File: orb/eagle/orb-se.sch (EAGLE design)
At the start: 27 parts, among them J1 MICRO USB, Q1 12MHZ, T1 DMG2302U, T2 DMG2302U, T3 DMG2302U, U1 ATINY44A

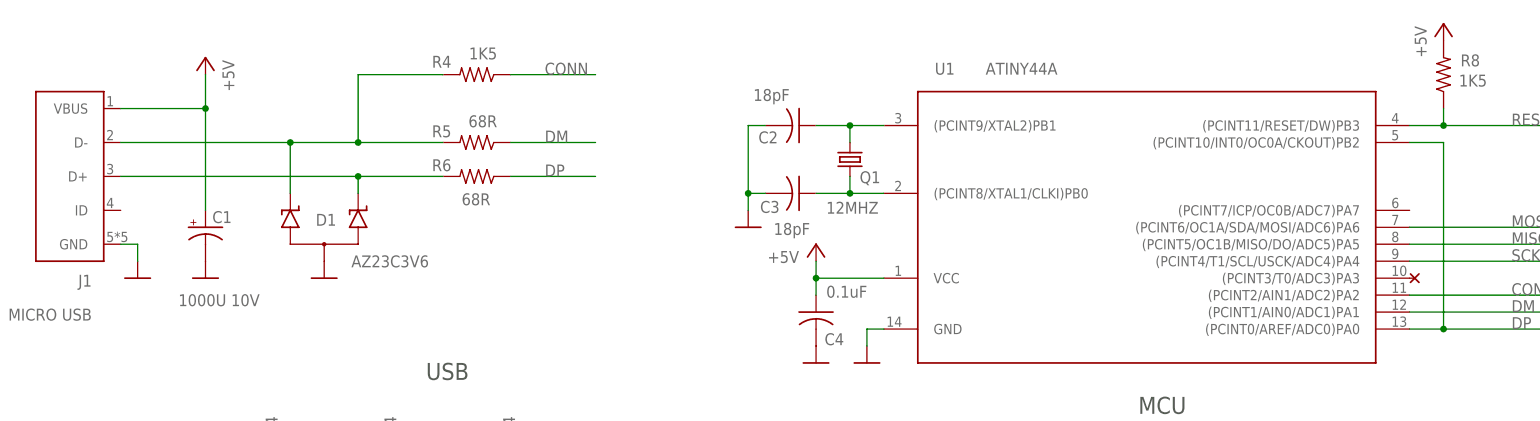
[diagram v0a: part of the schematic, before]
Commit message: Minor tweaks. Cleaned DRC errors. Verified netlist. Ready for final auto routing.
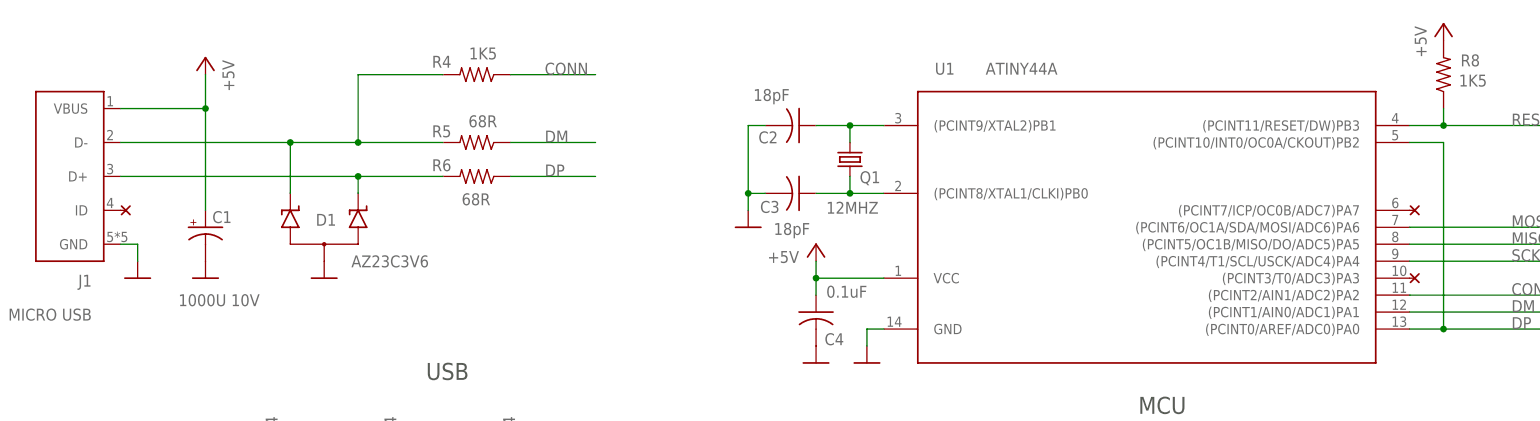
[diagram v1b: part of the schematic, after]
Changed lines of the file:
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@@
 <part name="+5V5" library="orb-se" deviceset="+5V" device=""/>
 <part name="+5V6" library="orb-se" deviceset="+5V" device=""/>
+<part name="NC$2" library="orb-se" deviceset="NC" device=""/>
+<part name="NC$3" library="orb-se" deviceset="NC" device=""/>
 </parts>
 <sheets>
@@
 <instance part="+5V5" gate="G$1" x="66.04" y="116.84"/>
 <instance part="+5V6" gate="G$1" x="83.82" y="116.84"/>
+<instance part="NC$2" gate="G$1" x="223.52" y="149.86" rot="R180"/>
+<instance part="NC$3" gate="G$1" x="30.48" y="149.86" rot="R180"/>
 </instances>
 <busses>
